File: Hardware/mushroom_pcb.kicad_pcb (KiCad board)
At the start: 2 copper layers, 153.2 x 125.5 mm, 55 parts, among them J1 Conn_01x04, J2 Conn_01x07_Pin, J3 Screw_Terminal_01x03, J4 Screw_Terminal_01x02, J5 Screw_Terminal_01x02, J6 Screw_Terminal_01x03, J7 Conn_01x03_Pin, J8 Conn_01x04_Pin, J9 Barrel_Jack, Q3 AO3400A, Q4 AO3400A, SW1 SW_Push, SW2 SW_Push, SW3 RotaryEncoder_Switch, U1 ESP32-WROOM-32E, U2 LM2596S-5, U3 ME6211C33M5

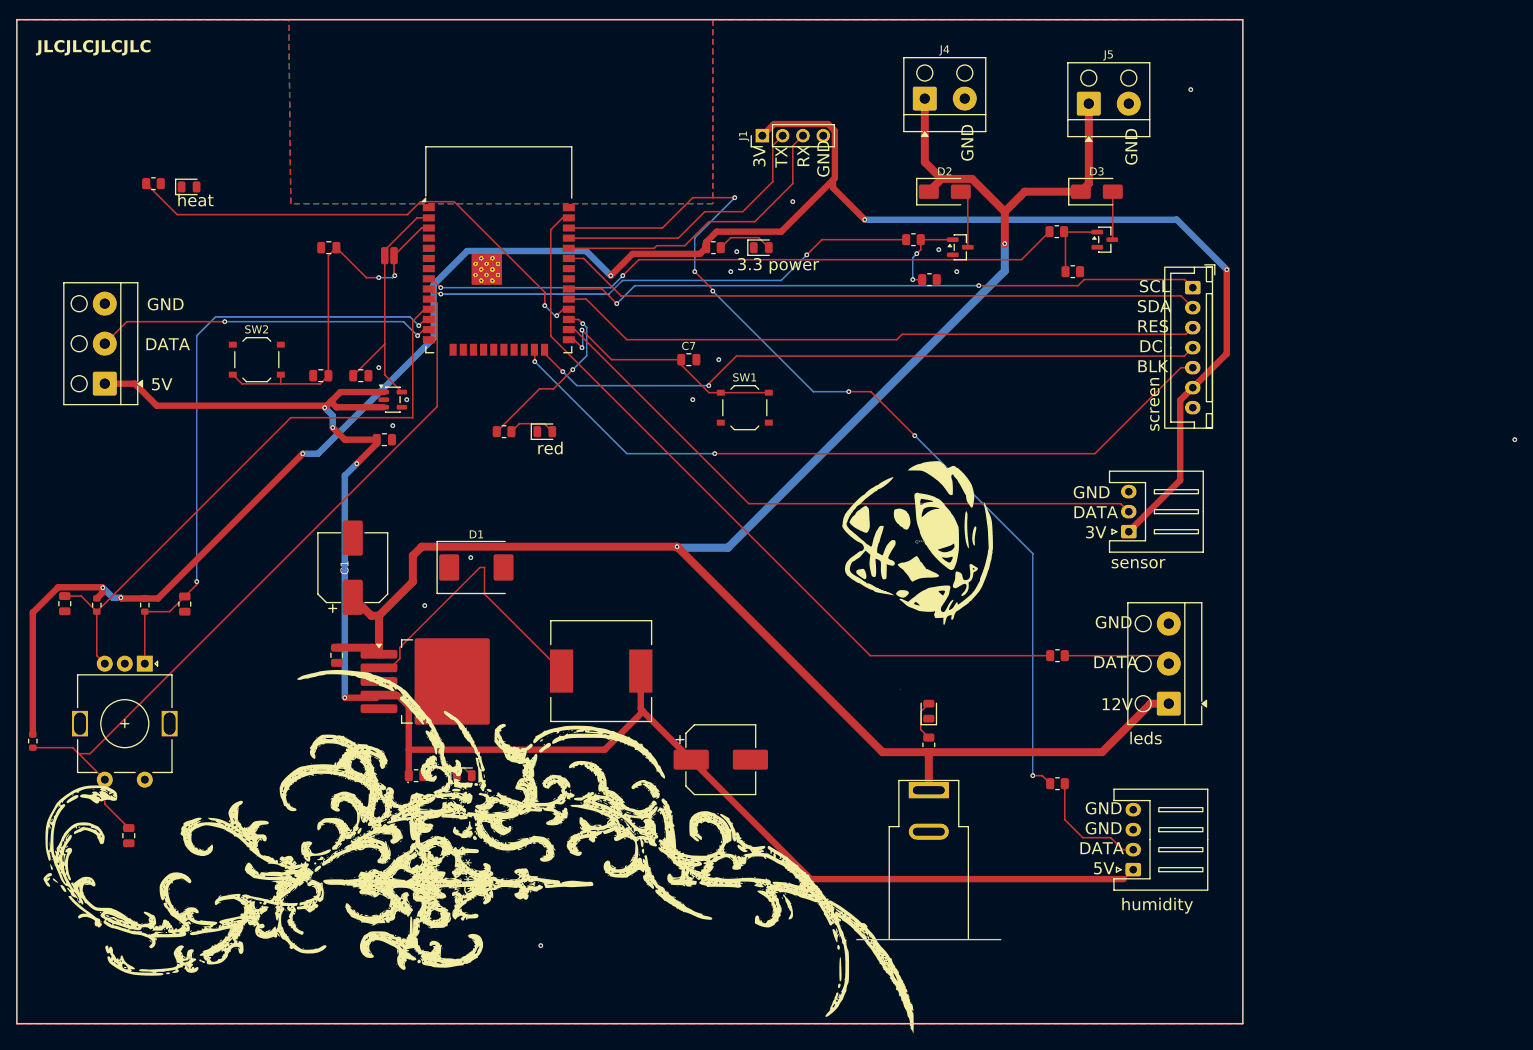
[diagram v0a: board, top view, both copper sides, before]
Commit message: Nueva version más compacta y con elementos handsoldering (falta rutear y cambiar algunas huellas)
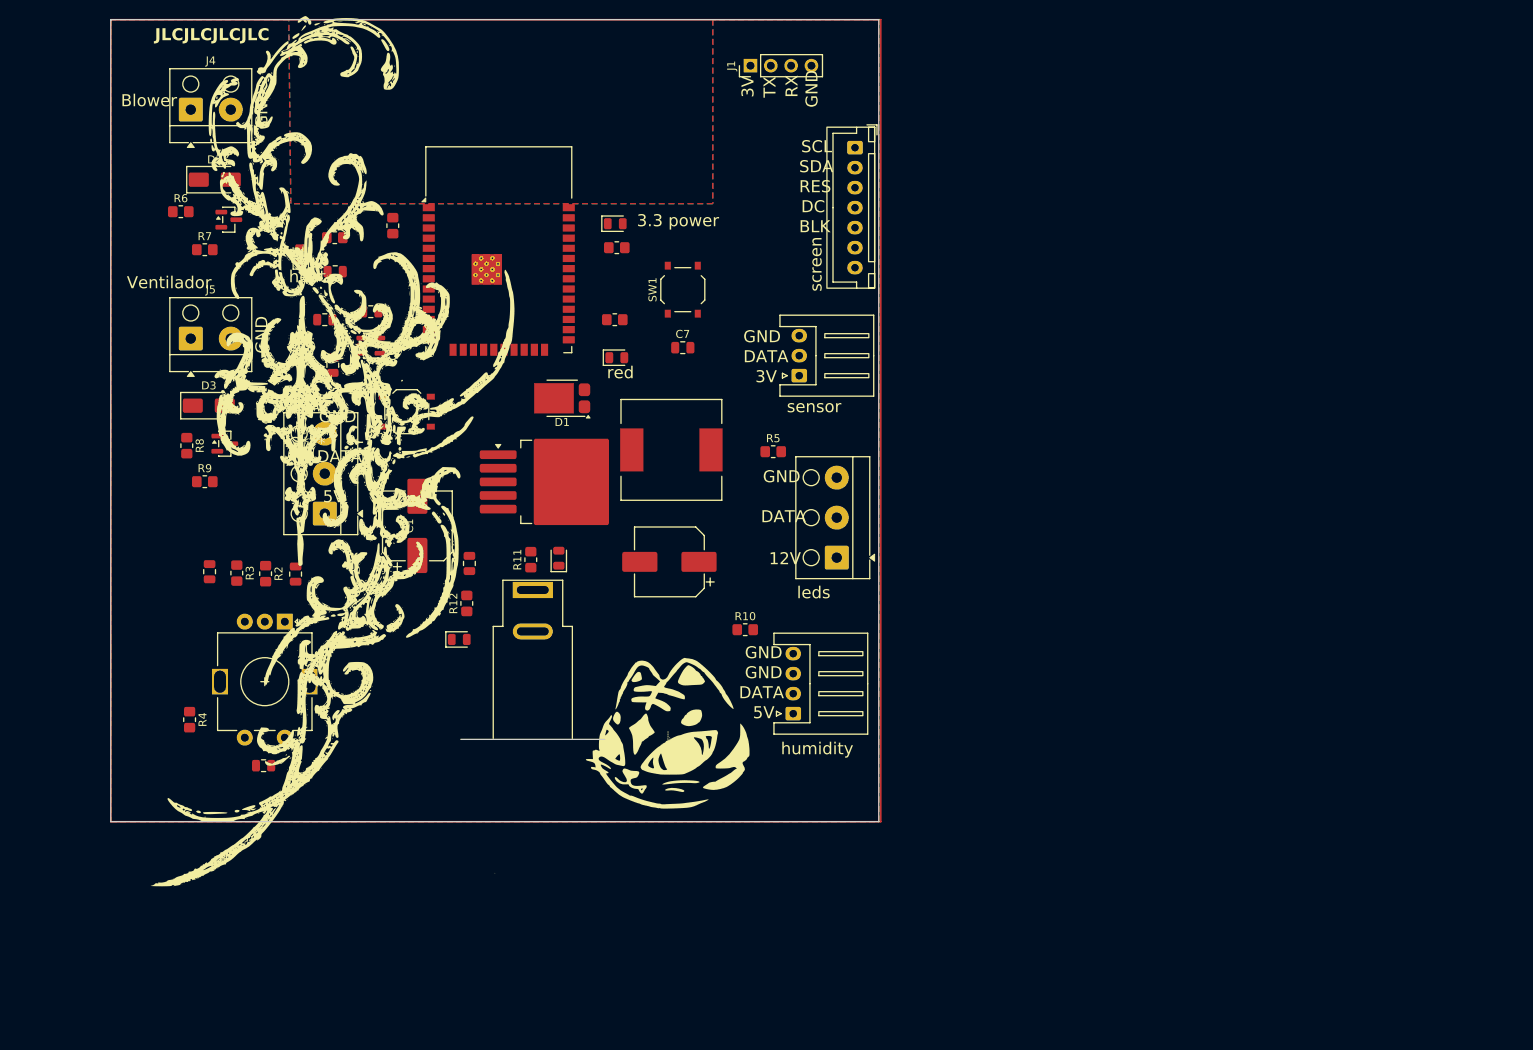
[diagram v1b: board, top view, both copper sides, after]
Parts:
- D1: value SS54 -> PMEG040V050EPD; footprint Diode_SMD:D_SMC -> Package_TO_SOT_SMD:Nexperia_CFP15_SOT-1289
- R1: footprint Resistor_SMD:R_0508_1220Metric -> Resistor_SMD:R_0805_2012Metric_Pad1.20x1.40mm_HandSolder
- R10, R11, R12, R13, R14, R15, R5, R6, R8: footprint Resistor_SMD:R_0805_2012Metric -> Resistor_SMD:R_0805_2012Metric_Pad1.20x1.40mm_HandSolder
- R2, R3, R4: footprint Resistor_SMD:R_0603_1608Metric -> Resistor_SMD:R_0805_2012Metric_Pad1.20x1.40mm_HandSolder
- R7, R9: value 10k -> R; footprint Resistor_SMD:R_0805_2012Metric -> Resistor_SMD:R_0805_2012Metric_Pad1.20x1.40mm_HandSolder
- moved J5 116.0 mm to (84.8, 73.1)
- moved D3 114.2 mm to (87.0, 81.5)
- moved Q4 112.9 mm to (89.0, 86.2)
- moved R8 112.0 mm to (84.2, 86.5), turned to -90 degrees
- moved R9 111.6 mm to (86.5, 91.0)
- moved J4 91.8 mm to (84.8, 44.5)
- moved R6 91.7 mm to (83.5, 57.2)
- moved Q3 91.5 mm to (89.5, 58.2)
- moved D2 91.3 mm to (87.8, 53.2)
- moved R7 90.7 mm to (86.5, 62.0)
- moved G*** 58.0 mm to (99.3, 86.2), turned to 0 degrees
- moved J9 55.5 mm to (127.5, 104.5)
- moved R11 54.9 mm to (127.2, 100.8)
- moved D4 50.0 mm to (130.8, 100.6)
- moved J8 46.8 mm to (160.1, 120.0)
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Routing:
- net +3V3: track 255.9 -> 0.00 mm, vias 6 -> 0
- net +12V: track 244.1 -> 0.00 mm, vias 2 -> 0
- net +5V: track 211.1 -> 0.00 mm, vias 4 -> 0
- net HUM: track 120.9 -> 0.00 mm, vias 6 -> 0
- net LED: track 95.1 -> 0.00 mm
- net SW: track 94.9 -> 0.00 mm
- net BLK: track 93.0 -> 0.00 mm, vias 2 -> 0
- net DC: track 85.3 -> 0.00 mm, vias 2 -> 0
- net FAN: track 80.9 -> 0.00 mm, vias 2 -> 0
- net RES: track 80.7 -> 0.00 mm
- net SDA: track 80.5 -> 0.00 mm
- net SCL: track 80.4 -> 0.00 mm, vias 2 -> 0
- net AMB: track 79.4 -> 0.00 mm
- net Net-(U1-IO27): track 76.9 -> 0.00 mm, vias 2 -> 0
- net Net-(U1-IO26): track 76.0 -> 0.00 mm
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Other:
- board size 153.2 x 125.5 mm -> 96 x 100.2 mm
- board text added: "Blower"
- board text added: "Ventilador"

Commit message: Re ruteo placa
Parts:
- moved R4 23.3 mm to (107.2, 126.2), turned to 0 degrees
- moved J6 23.2 mm to (82.2, 107.9)
- moved C10 21.5 mm to (88.7, 123.7), turned to 180 degrees
- moved C9 21.4 mm to (113.0, 116.9), turned to 90 degrees
- moved R3 17.9 mm to (88.9, 120.3), turned to 0 degrees
- moved R2 15.1 mm to (89.0, 116.7), turned to 0 degrees
- moved C11 13.6 mm to (89.0, 112.9), turned to 180 degrees
- moved Q4 8.79 mm to (80.2, 86.5)
- moved SW3 5.99 mm to (95.0, 114.3), turned to 0 degrees
- moved D3 4.54 mm to (82.5, 81.4)
- moved J5 4.54 mm to (80.2, 73.0)
- moved R9 4.54 mm to (82.0, 90.9)
- moved SW1 3.46 mm to (146.4, 70.5)
- moved C7 1.88 mm to (146.1, 76.1)
- moved R8 0.81 mm to (85.0, 86.3)
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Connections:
- U1 pad 23: BLK -> HUM
- U1 pad 24: DC -> LED
- U1 pad 30: SCL -> SDA
- U1 pad 33: SDA -> SCL
- U1 pad 36: HUM -> BLK
- U1 pad 37: LED -> DC
- U1 pad 8: FAN -> BLOW
- U1 pad 9: BLOW -> FAN
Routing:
- net +3V3: track 0.00 -> 214.0 mm, vias 0 -> 3
- net +12V: track 0.00 -> 165.7 mm, vias 0 -> 4
- net +5V: track 0.00 -> 163.4 mm, vias 0 -> 8
- net Net-(U1-IO26): track 0.00 -> 67.5 mm, vias 0 -> 2
- net SW: track 0.00 -> 63.6 mm
- net Net-(U1-IO27): track 0.00 -> 61.3 mm, vias 0 -> 2
- net HUM: track 0.00 -> 48.4 mm
- net HEAT: track 0.00 -> 45.6 mm, vias 0 -> 2
- net Net-(J1-Pin_3): track 0.00 -> 42.8 mm, vias 0 -> 2
- net SDA: track 0.00 -> 42.1 mm
- net RES: track 0.00 -> 41.5 mm
- net SCL: track 0.00 -> 41.5 mm
- net Net-(J1-Pin_2): track 0.00 -> 40.6 mm
- net BLOW: track 0.00 -> 39.8 mm, vias 0 -> 2
- net LED_TERM: track 0.00 -> 37.7 mm
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
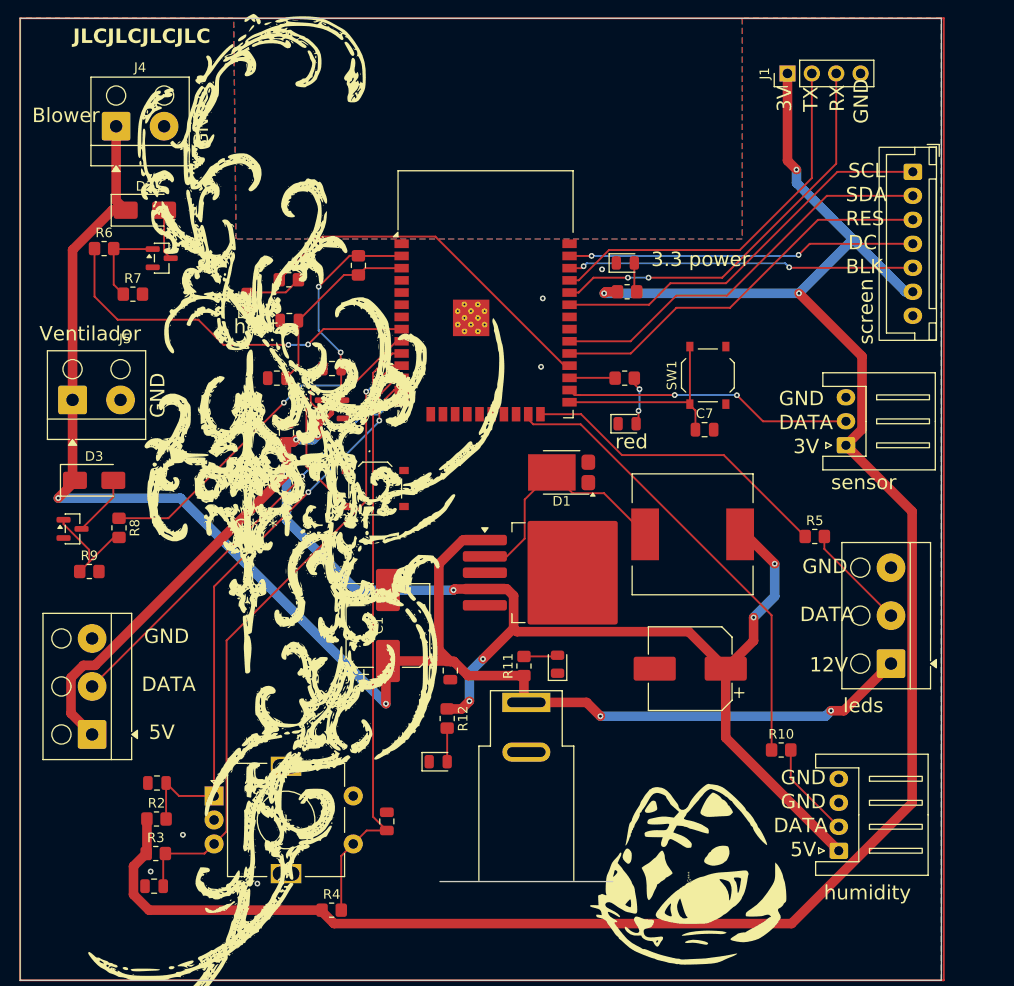
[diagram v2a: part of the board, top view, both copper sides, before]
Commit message: cambio de conectores + octoacoplador calentador
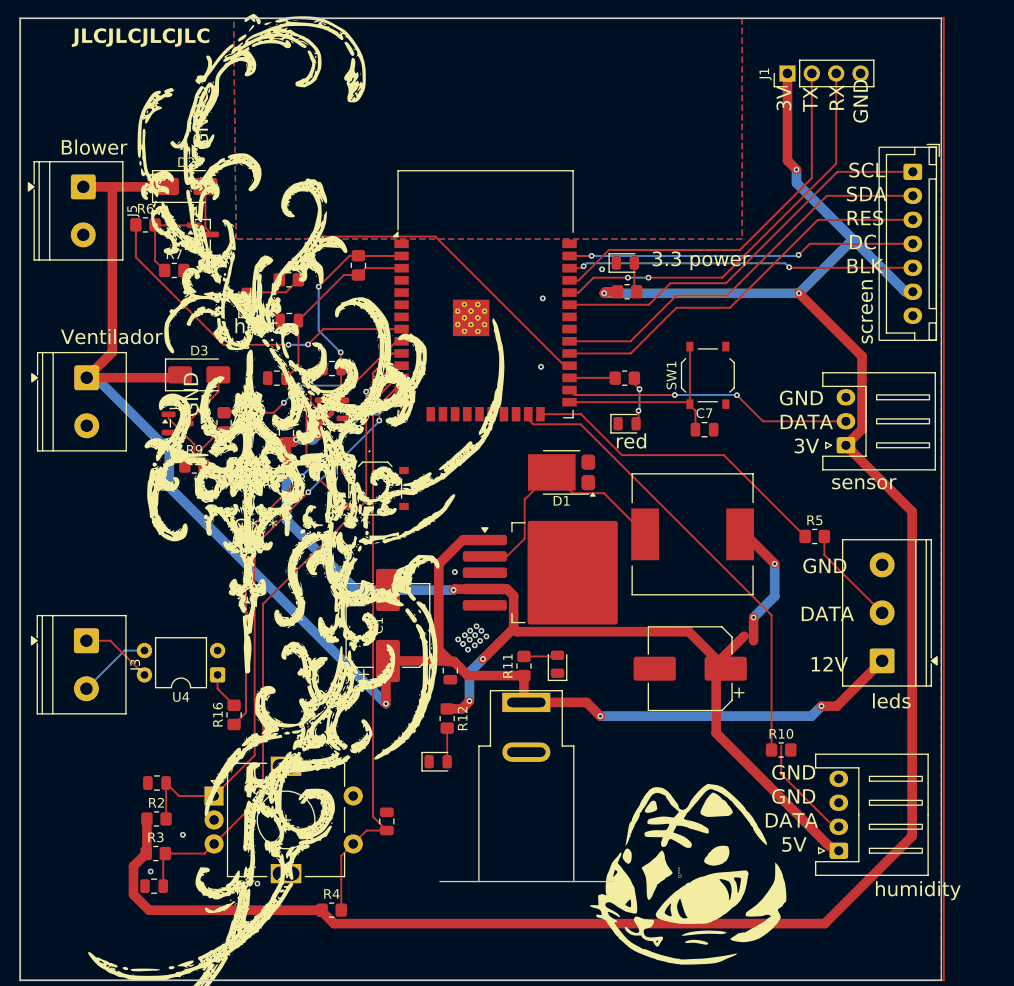
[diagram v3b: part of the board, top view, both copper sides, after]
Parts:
- removed J4: Screw_Terminal_01x02, TerminalBlock_Altech:Altech_AK100_1x02_P5.00mm
- added J10: Screw_Terminal_01x03, TerminalBlock_Phoenix:TerminalBlock_Phoenix_PT-1,5-3-5.0-H_1x03_P5.00mm_Horizontal, F.Cu at (164.6, 100.2)
- added R16: 680, Resistor_SMD:R_0805_2012Metric_Pad1.20x1.40mm_HandSolder, F.Cu at (97.0, 105.8)
- added U4: PC817, Package_DIP:DIP-4_W7.62mm, F.Cu at (95.3, 101.7)
- J3, J6: value Screw_Terminal_01x03 -> Screw_Terminal_01x02; footprint TerminalBlock_Altech:Altech_AK100_1x03_P5.00mm -> TerminalBlock_Phoenix:TerminalBlock_Phoenix_PT-1,5-2-5.0-H_1x02_P5.00mm_Horizontal
- J5: footprint TerminalBlock_Altech:Altech_AK100_1x02_P5.00mm -> TerminalBlock_Phoenix:TerminalBlock_Phoenix_PT-1,5-2-5.0-H_1x02_P5.00mm_Horizontal
- R7, R9: value R -> 10k
- moved J3 83.9 mm to (81.7, 98.1), turned to -90 degrees
- moved J6 37.2 mm to (81.7, 70.7), turned to -90 degrees
- moved J5 22.2 mm to (81.3, 50.8), turned to -90 degrees
- moved G*** 21.1 mm to (144.3, 78.0)
- moved D3 15.5 mm to (93.4, 70.4)
- moved R9 15.5 mm to (92.9, 79.9)
- moved Q4 15.5 mm to (91.2, 75.5)
- moved R8 15.5 mm to (96.0, 75.4)
- moved D2 4.97 mm to (92.1, 50.8)
- moved Q3 4.97 mm to (93.8, 55.8)
- moved R6 4.97 mm to (87.8, 54.8)
- moved R7 4.97 mm to (90.8, 59.5)
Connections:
- J3 pad 1: +12V -> Net-(J3-Pin_1)
- J6 pad 1: +5V -> +12V
- J6 pad 2: HEAT -> GND
- R5 pad 2: Net-(J3-Pin_2) -> Net-(J10-Pin_2)
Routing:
- net +5V: track 163.4 -> 125.3 mm
- net FAN: track 37.1 -> 21.6 mm
- net Net-(J10-Pin_2): track 0.00 -> 10.5 mm
- net Net-(J3-Pin_1): track 0.00 -> 7.52 mm
- net BLOW: track 39.8 -> 35.5 mm
- net Net-(R16-Pad2): track 0.00 -> 3.88 mm
- net Net-(J3-Pin_2): track 11.1 -> 7.70 mm
- net HEAT: track 45.6 -> 43.5 mm
- net +3V3: track 214.0 -> 216.0 mm
- net +12V: track 165.7 -> 166.4 mm, vias 4 -> 3
- net GND: vias 8 -> 21

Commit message: cambios menores, conectores + octo
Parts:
- J9: footprint Connector_BarrelJack:BarrelJack_SwitchcraftConxall_RAPC10U_Horizontal -> Connector_BarrelJack:BarrelJack_CUI_PJ-102AH_Horizontal
- moved J9 13.5 mm to (127.5, 118.0), turned to 0 degrees
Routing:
- net +12V: track 166.4 -> 178.6 mm

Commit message: Cambios en arch de fabricacion
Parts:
- removed D1: PMEG040V050EPD, Package_TO_SOT_SMD:Nexperia_CFP15_SOT-1289
- added D9: SS54, Diode_SMD:D_SMA, F.Cu at (131.9, 81.2)
- moved G*** 20.5 mm to (125.3, 85.7)
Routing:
- net Net-(D9-K): track 25.4 -> 24.7 mm
- net GND: vias 21 -> 76
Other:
- board text added: "Fan"
- board text added: "Heater"
- board text removed: "Ventilador"
